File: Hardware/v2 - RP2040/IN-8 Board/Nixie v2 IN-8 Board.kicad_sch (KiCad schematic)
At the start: 16 parts, among them J1 Conn_01x10_Socket, J2 Conn_01x10_Socket, J3 Conn_01x10_Socket, Q1 MMBTA42, Q2 PZTA92, U1 NCH8200HV

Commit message: seperated the processor and nixie boards
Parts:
- removed J1, J2, J3: Conn_01x10_Socket, symbol Connector:Conn_01x10_Socket
- removed TP3: TestPoint, symbol Connector:TestPoint
- added C3: 100n, symbol Device:C_Small
- added C4: 10u, symbol Device:C_Polarized_Small_US
- added J1, J2, J3: Conn_01x10_Pin, symbol Connector:Conn_01x10_Pin
- added N1, N2, N3, N4: ИN-8, symbol Nick_Nixie:ИN-8
- added R11, R7, R8, R9: 22k, symbol Device:R_Small_US
- added R6: 10k, symbol Device:R_Small_US
- added U2: VEML7700, symbol Nick_Sensor:VEML7700
- added U3, U4, U5, U6: К155ИД1, symbol Nick_Nixie:К155ИД1
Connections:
- net ANODE: now also R11.1, R7.1, R8.1, R9.1
- net DIMMING: now also J3.5 (Pin_5)
- net GND: now also C3.2, C4.2, J1.1 (Pin_1), J1.10 (Pin_10), J2.1 (Pin_1), J2.10 (Pin_10), J3.1 (Pin_1), J3.2 (Pin_2), U2.3 (GND), U3.12 (GND), U4.12 (GND), U5.12 (GND), U6.12 (GND)
- net VBUS: now also J3.10 (Pin_10), J3.9 (Pin_9), U3.5 (Vcc), U4.5 (Vcc), U5.5 (Vcc), U6.5 (Vcc)
- net at TP2.1: now also J3.4 (Pin_4)
- net at TP1.1: now also J3.3 (Pin_3)
- new net: N3.11 (Anode), R9.2
- new net: N1.11 (Anode), R7.2
- new net: N2. (5), U4.14 (5)
- new net: N2.1, U4.15 (1)
- new net: N2.10 (0), U4.16 (0)
- new net: N2.11 (Anode), R8.2
- new net: N2.2, U4.8 (2)
- new net: N2.3, U4.9 (3)
- new net: N2.4, U4.13 (4)
- new net: N2.6, U4.11 (6)
- new net: N2.7, U4.10 (7)
- new net: N2.8, U4.1 (8)
- new net: N2.9, U4.8 (2)
- new net: C3.1, C4.1, R6.1, U2.2 (Vdd)
- new net: N3.8, U5.1 (8)
- new net: N3.7, U5.10 (7)
- new net: N3.6, U5.11 (6)
- new net: N3.4, U5.13 (4)
- new net: N3. (5), U5.14 (5)
- new net: N3.1, U5.15 (1)
- new net: N3.10 (0), U5.16 (0)
- new net: N3.2, U5.8 (2)
- new net: N3.9, U5.8 (2)
- new net: N3.3, U5.9 (3)
- new net: N4. (5), U6.14 (5)
- new net: N4.1, U6.15 (1)
- new net: N4.10 (0), U6.16 (0)
- new net: N4.11 (Anode), R11.2
- new net: N4.2, U6.8 (2)
- new net: N4.3, U6.9 (3)
- new net: N4.4, U6.13 (4)
- new net: N4.6, U6.11 (6)
- new net: N4.7, U6.10 (7)
- new net: N4.8, U6.1 (8)
- new net: N4.9, U6.8 (2)
- new net: N1.8, U3.1 (8)
- new net: N1.7, U3.10 (7)
- new net: N1.6, U3.11 (6)
- new net: N1.4, U3.13 (4)
- new net: N1. (5), U3.14 (5)
- new net: N1.1, U3.15 (1)
- new net: N1.10 (0), U3.16 (0)
- new net: N1.2, U3.8 (2)
- new net: N1.9, U3.8 (2)
- new net: N1.3, U3.9 (3)
- new net +3V3: J3.8 (Pin_8), R6.2
- new net Hours_Ones_A: J1.2 (Pin_2), U4.3 (A)
- new net Hours_Ones_B: J1.4 (Pin_4), U4.6 (B)
- new net Hours_Ones_C: J1.5 (Pin_5), U4.7 (C)
- new net Hours_Ones_D: J1.3 (Pin_3), U4.4 (D)
- new net Hours_Tens_A: J1.9 (Pin_9), U3.3 (A)
- new net Hours_Tens_B: J1.7 (Pin_7), U3.6 (B)
- new net Hours_Tens_C: J1.6 (Pin_6), U3.7 (C)
- new net Hours_Tens_D: J1.8 (Pin_8), U3.4 (D)
- new net I2C1_SCL: J3.6 (Pin_6), U2.1 (SCL)
- new net I2C1_SDA: J3.7 (Pin_7), U2.4 (SDA)
- new net Minutes_Ones_A: J2.2 (Pin_2), U6.3 (A)
- new net Minutes_Ones_B: J2.4 (Pin_4), U6.6 (B)
- new net Minutes_Ones_C: J2.5 (Pin_5), U6.7 (C)
- new net Minutes_Ones_D: J2.3 (Pin_3), U6.4 (D)
- new net Minutes_Tens_A: J2.9 (Pin_9), U5.3 (A)
- new net Minutes_Tens_B: J2.7 (Pin_7), U5.6 (B)
- new net Minutes_Tens_C: J2.6 (Pin_6), U5.7 (C)
- new net Minutes_Tens_D: J2.8 (Pin_8), U5.4 (D)
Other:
- note added: "LIGHT SENSOR"
- note added: "NIXIE BOARD INTERFACE"
- note added: "NIXIE POWER AND DIMMING"
- note added: "NIXIE TUBES AND DRIVERS"
- title: (none) -> ИN-8 Display Board
- moved on the sheet: C1, C2, Q1, Q2, R1, R2, R3, R4, R5, TP1, TP2, U1

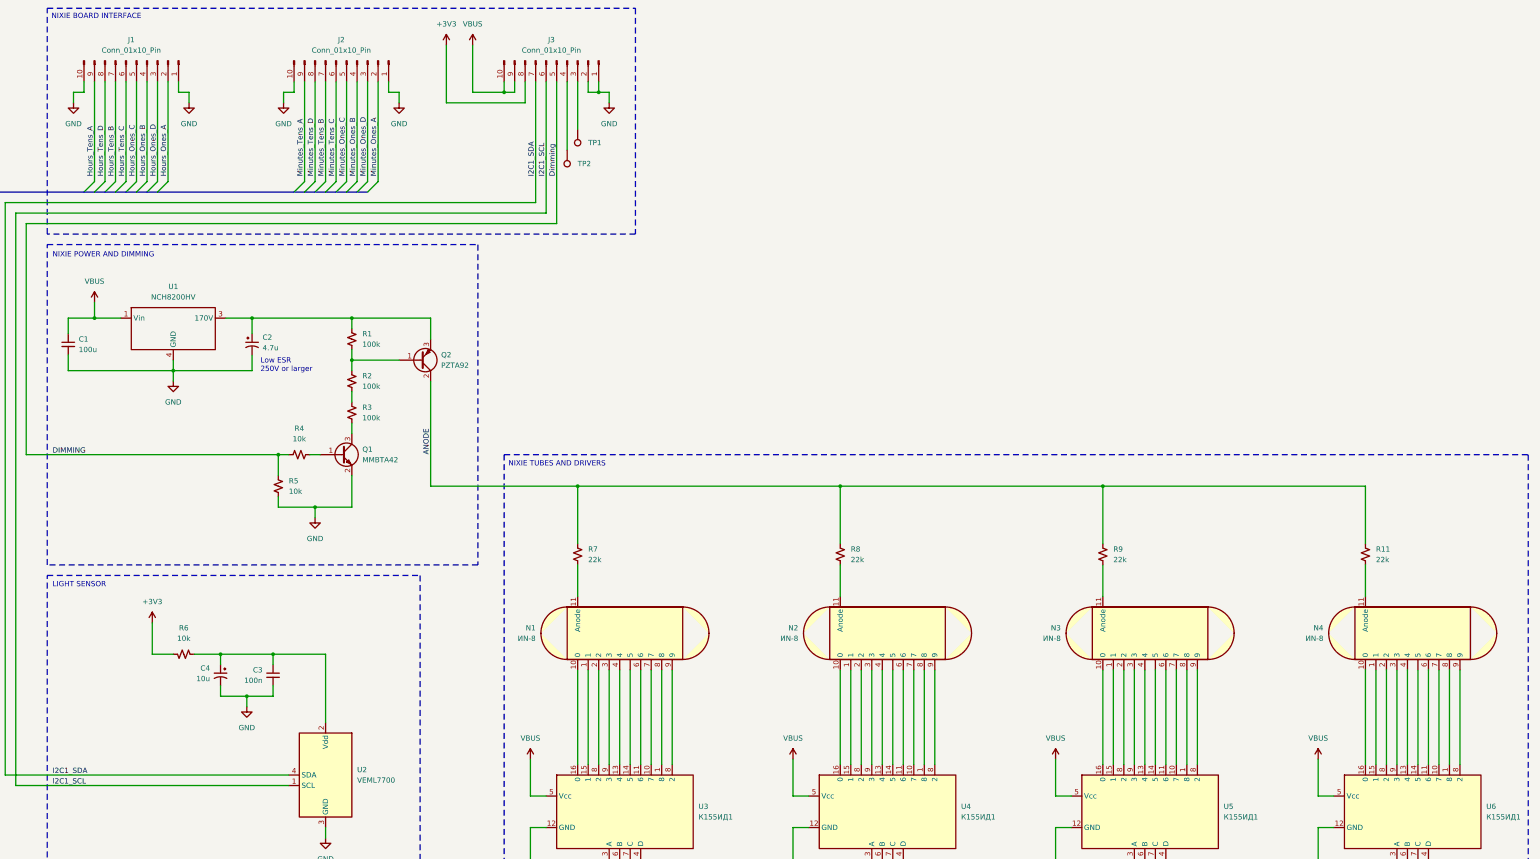
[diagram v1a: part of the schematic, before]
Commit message: Assigned footprints
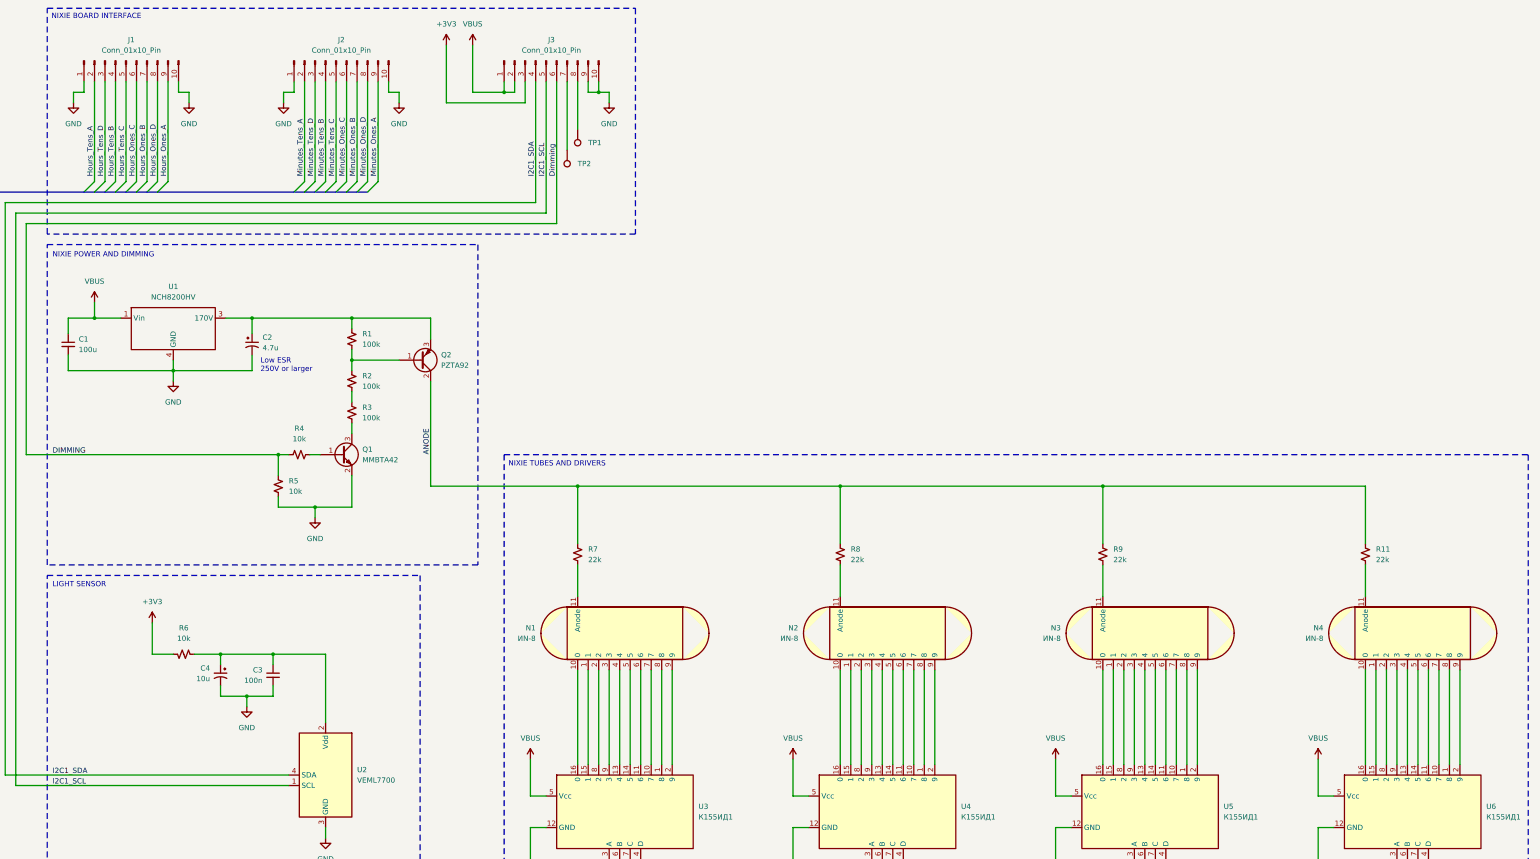
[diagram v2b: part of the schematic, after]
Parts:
- C1, C3: footprint (none) -> Capacitor_SMD:C_0603_1608Metric
- J1, J2, J3: footprint (none) -> Connector_PinHeader_2.54mm:PinHeader_2x05_P2.54mm_Horizontal
- N1, N2, N3, N4: footprint (none) -> Nick_Nixie:ИN-8
- R1, R2, R3, R4, R5, R6: footprint (none) -> Resistor_SMD:R_0603_1608Metric
- R11, R7, R8, R9: footprint (none) -> Resistor_SMD:R_0805_2012Metric
- U1: footprint (none) -> Nick_Nixie:NCH8200HV
- U3, U4, U5, U6: footprint (none) -> Package_DIP:DIP-16_W7.62mm
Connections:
- net +3V3: now also J3.3 (Pin_3); no longer J3.8 (Pin_8)
- net DIMMING: now also J3.6 (Pin_6); no longer J3.5 (Pin_5)
- net GND: now also J3.10 (Pin_10), J3.9 (Pin_9); no longer J3.1 (Pin_1), J3.2 (Pin_2)
- net Hours_Ones_A: now also J1.9 (Pin_9); no longer J1.2 (Pin_2)
- net Hours_Ones_B: now also J1.7 (Pin_7); no longer J1.4 (Pin_4)
- net Hours_Ones_C: now also J1.6 (Pin_6); no longer J1.5 (Pin_5)
- net Hours_Ones_D: now also J1.8 (Pin_8); no longer J1.3 (Pin_3)
- net Hours_Tens_A: now also J1.2 (Pin_2); no longer J1.9 (Pin_9)
- net Hours_Tens_B: now also J1.4 (Pin_4); no longer J1.7 (Pin_7)
- net Hours_Tens_C: now also J1.5 (Pin_5); no longer J1.6 (Pin_6)
- net Hours_Tens_D: now also J1.3 (Pin_3); no longer J1.8 (Pin_8)
- net I2C1_SCL: now also J3.5 (Pin_5); no longer J3.6 (Pin_6)
- net I2C1_SDA: now also J3.4 (Pin_4); no longer J3.7 (Pin_7)
- net Minutes_Ones_A: now also J2.9 (Pin_9); no longer J2.2 (Pin_2)
- net Minutes_Ones_B: now also J2.7 (Pin_7); no longer J2.4 (Pin_4)
- net Minutes_Ones_C: now also J2.6 (Pin_6); no longer J2.5 (Pin_5)
- net Minutes_Ones_D: now also J2.8 (Pin_8); no longer J2.3 (Pin_3)
- net Minutes_Tens_A: now also J2.2 (Pin_2); no longer J2.9 (Pin_9)
- net Minutes_Tens_B: now also J2.4 (Pin_4); no longer J2.7 (Pin_7)
- net Minutes_Tens_C: now also J2.5 (Pin_5); no longer J2.6 (Pin_6)
- net Minutes_Tens_D: now also J2.3 (Pin_3); no longer J2.8 (Pin_8)
- net VBUS: now also J3.1 (Pin_1), J3.2 (Pin_2); no longer J3.10 (Pin_10), J3.9 (Pin_9)
- net at U4.14 (5): now also N2.5; no longer N2. (5)
- net at N2.9: now also U4.2 (9); no longer U4.8 (2)
- net at U5.14 (5): now also N3.5; no longer N3. (5)
- net at N3.9: now also U5.2 (9); no longer U5.8 (2)
- net at U6.14 (5): now also N4.5; no longer N4. (5)
- net at N4.9: now also U6.2 (9); no longer U6.8 (2)
- net at U3.14 (5): now also N1.5; no longer N1. (5)
- net at N1.9: now also U3.2 (9); no longer U3.8 (2)
- net at TP2.1: now also J3.7 (Pin_7); no longer J3.4 (Pin_4)
- net at TP1.1: now also J3.8 (Pin_8); no longer J3.3 (Pin_3)

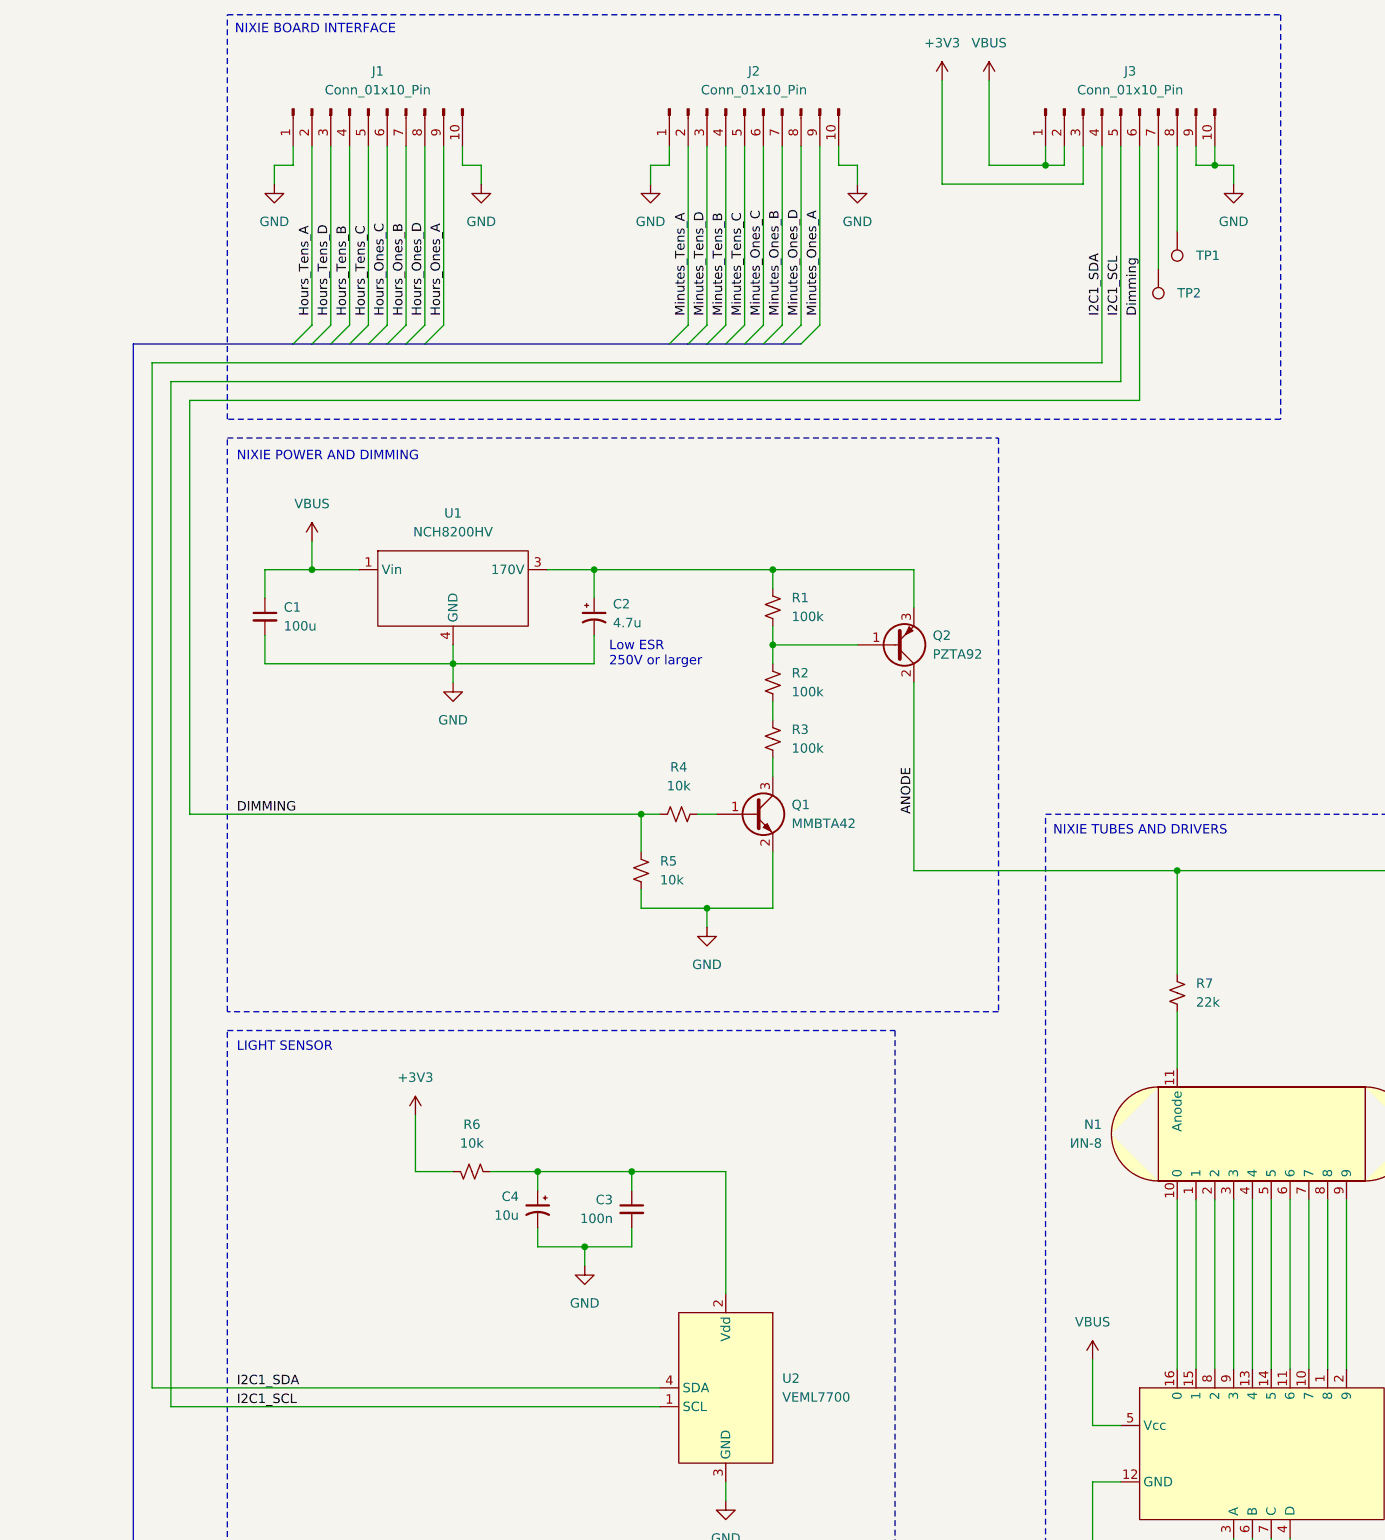
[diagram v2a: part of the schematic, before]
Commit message: Started board layout
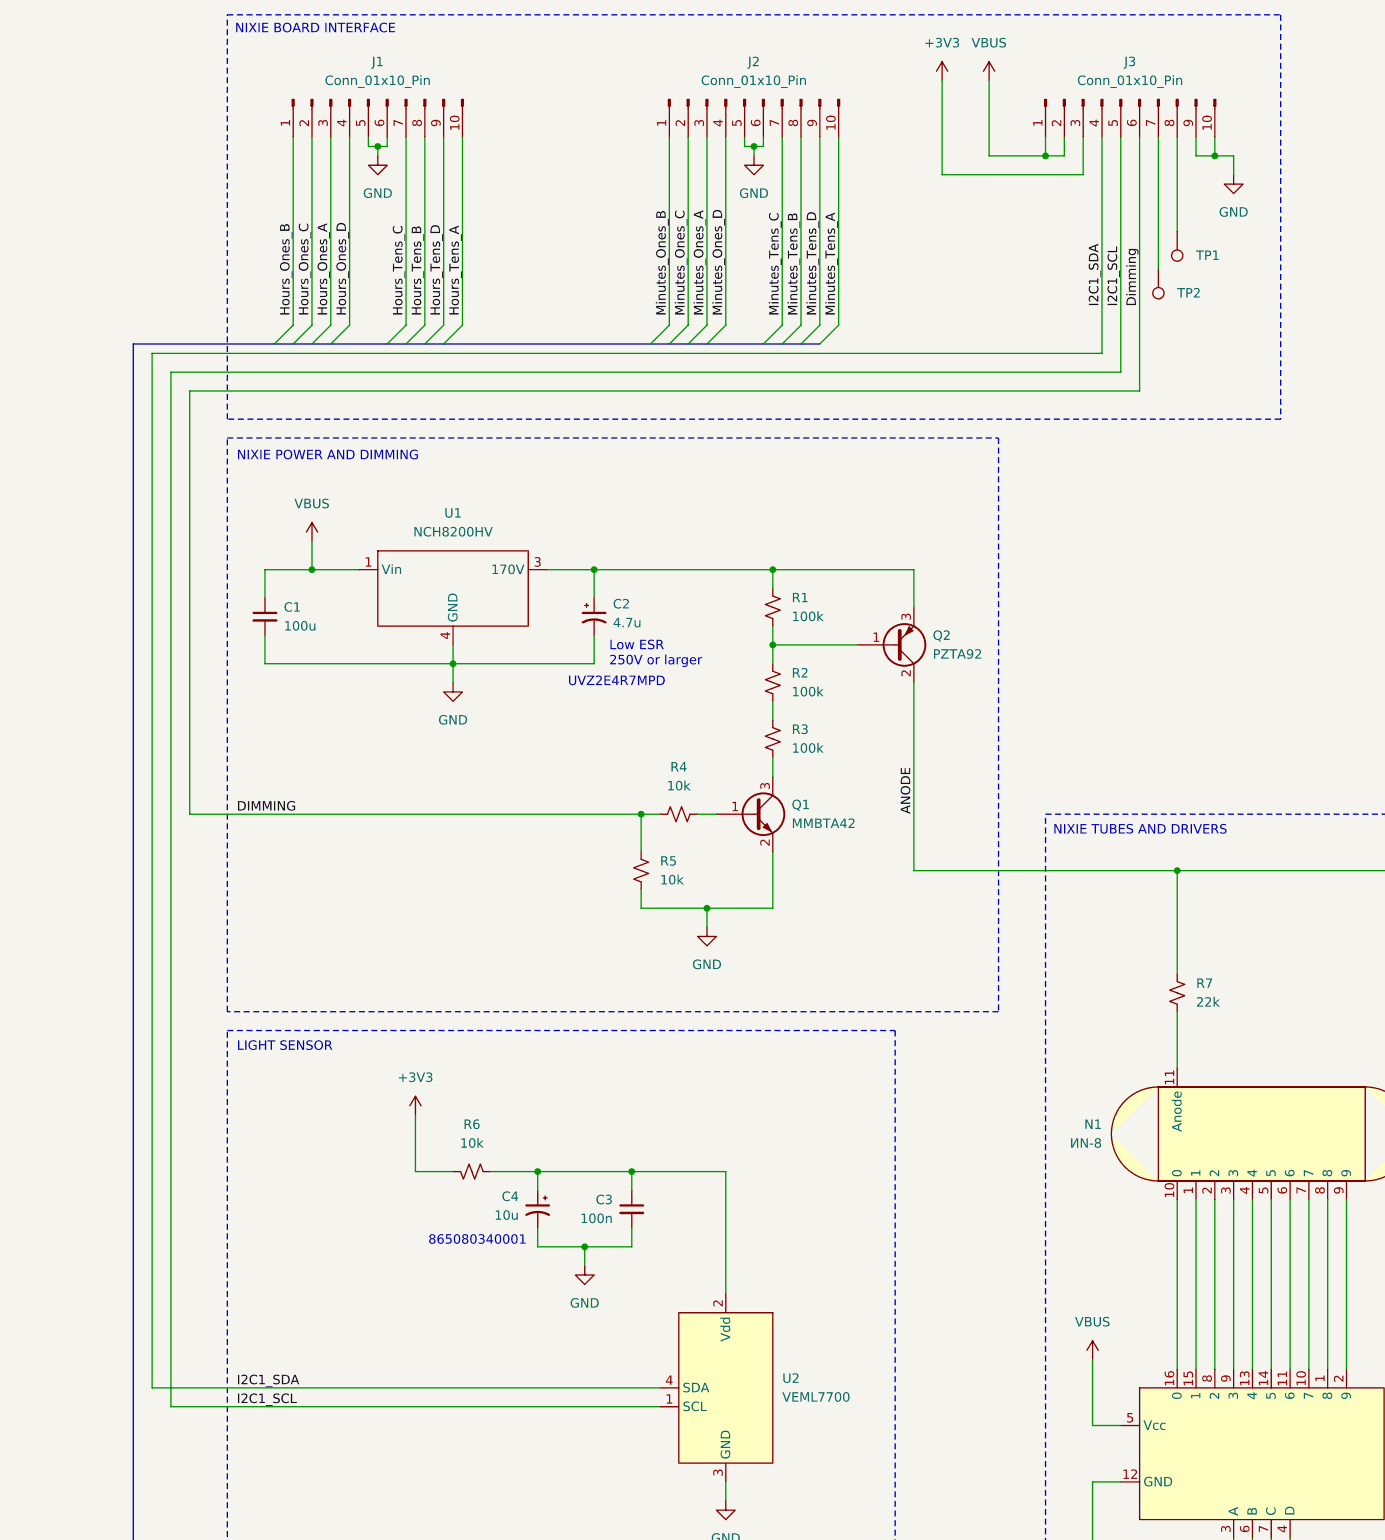
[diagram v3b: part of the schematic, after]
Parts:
- C2: footprint (none) -> Capacitor_THT:CP_Radial_D8.0mm_P3.50mm
- C4: footprint (none) -> Capacitor_SMD:CP_Elec_4x5.4
- TP1, TP2: footprint (none) -> TestPoint:TestPoint_Pad_D2.0mm
- U2: footprint (none) -> Nick_Sensors:VEML7700-TV
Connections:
- net GND: now also J1.5 (Pin_5), J1.6 (Pin_6), J2.5 (Pin_5), J2.6 (Pin_6); no longer J1.1 (Pin_1), J1.10 (Pin_10), J2.1 (Pin_1), J2.10 (Pin_10)
- net Hours_Ones_A: now also J1.3 (Pin_3); no longer J1.9 (Pin_9)
- net Hours_Ones_B: now also J1.1 (Pin_1); no longer J1.7 (Pin_7)
- net Hours_Ones_C: now also J1.2 (Pin_2); no longer J1.6 (Pin_6)
- net Hours_Ones_D: now also J1.4 (Pin_4); no longer J1.8 (Pin_8)
- net Hours_Tens_A: now also J1.10 (Pin_10); no longer J1.2 (Pin_2)
- net Hours_Tens_B: now also J1.8 (Pin_8); no longer J1.4 (Pin_4)
- net Hours_Tens_C: now also J1.7 (Pin_7); no longer J1.5 (Pin_5)
- net Hours_Tens_D: now also J1.9 (Pin_9); no longer J1.3 (Pin_3)
- net Minutes_Ones_A: now also J2.3 (Pin_3); no longer J2.9 (Pin_9)
- net Minutes_Ones_B: now also J2.1 (Pin_1); no longer J2.7 (Pin_7)
- net Minutes_Ones_C: now also J2.2 (Pin_2); no longer J2.6 (Pin_6)
- net Minutes_Ones_D: now also J2.4 (Pin_4); no longer J2.8 (Pin_8)
- net Minutes_Tens_A: now also J2.10 (Pin_10); no longer J2.2 (Pin_2)
- net Minutes_Tens_B: now also J2.8 (Pin_8); no longer J2.4 (Pin_4)
- net Minutes_Tens_C: now also J2.7 (Pin_7); no longer J2.5 (Pin_5)
- net Minutes_Tens_D: now also J2.9 (Pin_9); no longer J2.3 (Pin_3)
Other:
- note added: "865080340001"
- note added: "UVZ2E4R7MPD"
- moved on the sheet: J1, J2, J3
